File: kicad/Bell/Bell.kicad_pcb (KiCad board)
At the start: 2 copper layers, 50.6 x 40.5 mm, 14 parts, among them J1 Jack-DC, Q1 Q_NMOS_GDS, U1 NodeMCUv3

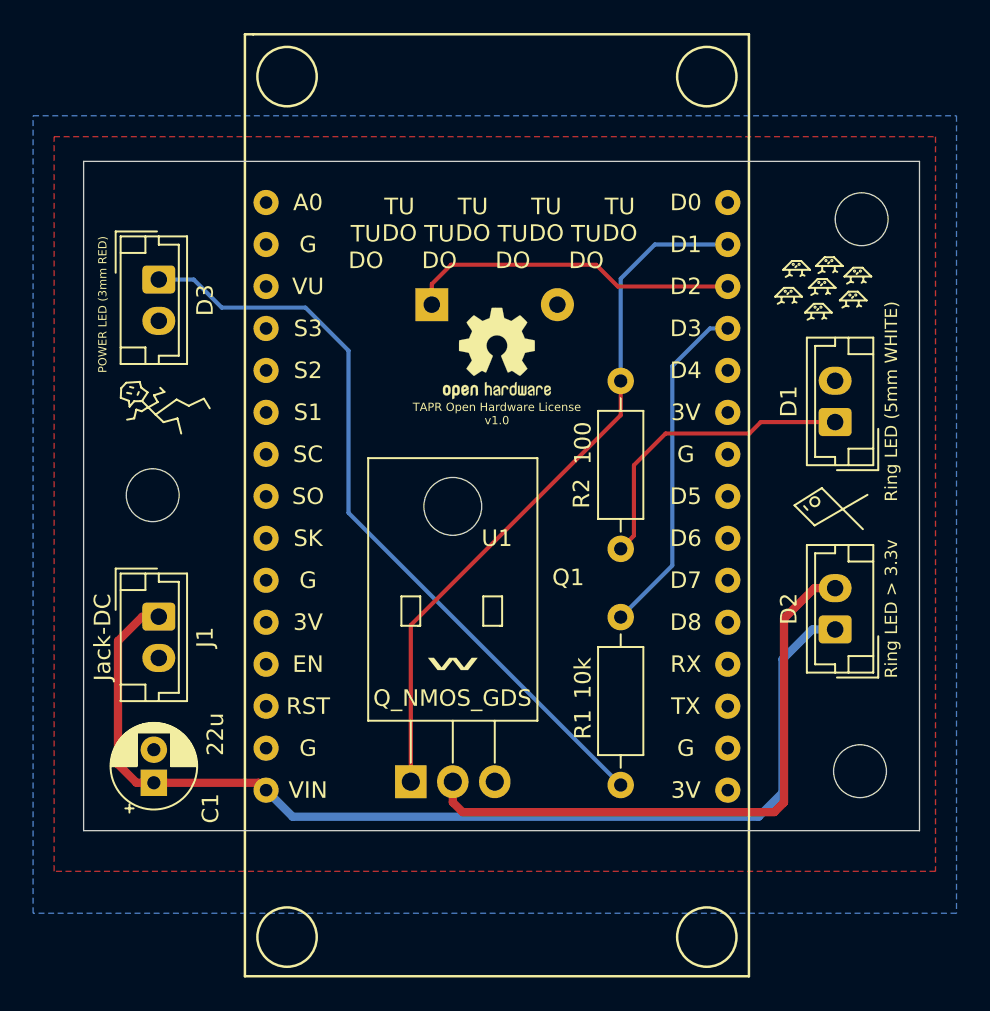
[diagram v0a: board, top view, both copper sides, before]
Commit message: Git: Ignore kicad backups and cache files
Signed-off-by: CTXz <ctx.xda@gmail.com>
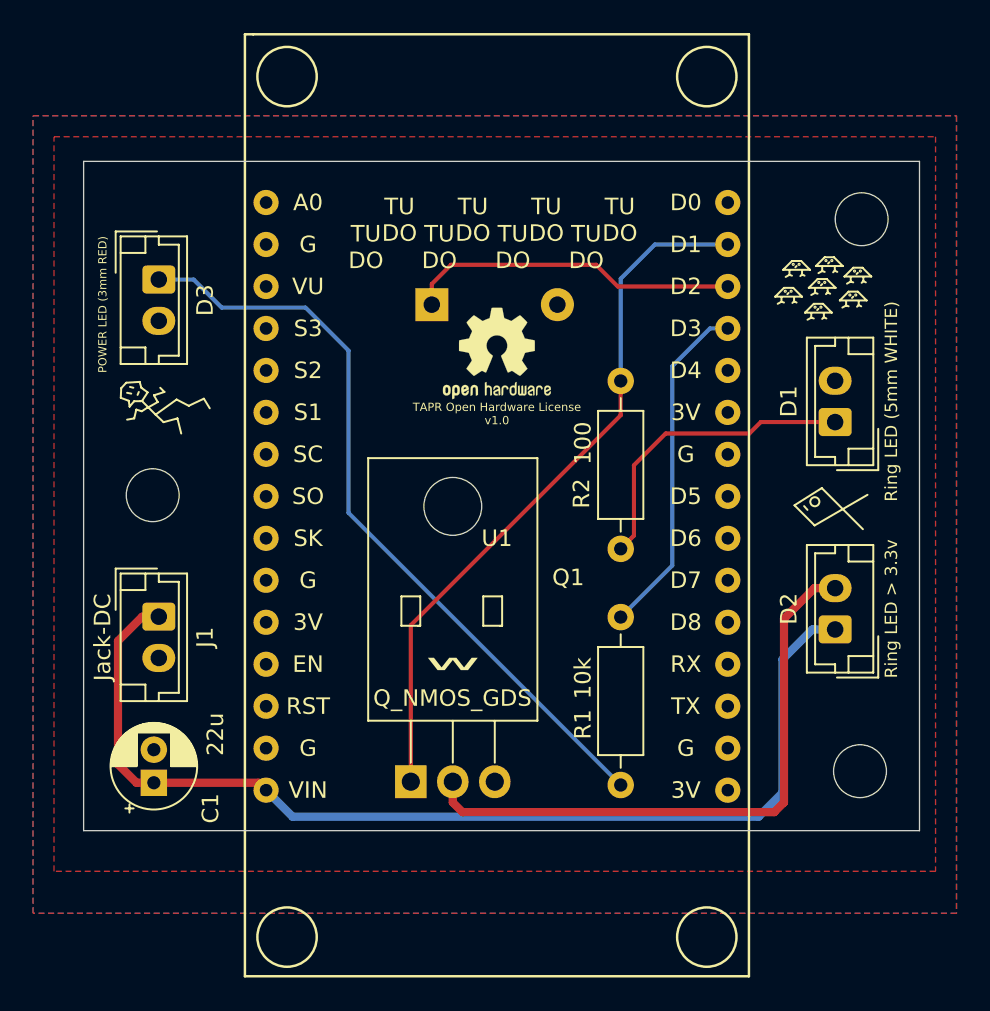
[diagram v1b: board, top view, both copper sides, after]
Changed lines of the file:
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@@
   (segment (start 135.419999 91.446701) (end 135.419999 87.185601) (width 0.25) (layer "F.Cu") (net 27))
   (segment (start 143.09806 84.57484) (end 142.4051 85.2678) (width 0.25) (layer "F.Cu") (net 27))
+  (zone (net 1) (net_name "GND") (layers F&B.Cu) (hatch edge 0.508)
+    (connect_pads (clearance 0.508))
+    (min_thickness 0.254) (filled_areas_thickness no)
+    (fill yes (thermal_gap 0.508) (thermal_bridge_width 0.508))
+    (polygon
+      (pts
+        (xy 154.94 114.3)
+        (xy 99.06 114.3)
+        (xy 99.06 66.04)
+        (xy 154.94 66.04)
+      )
+    )
+  )
   (zone (net 1) (net_name "GND") (layer "F.Cu") (hatch edge 0.508)
     (connect_pads (clearance 0.508))
-    (min_thickness 0.254)
+    (min_thickness 0.254) (filled_areas_thickness no)
     (fill yes (thermal_gap 0.508) (thermal_bridge_width 0.508))
     (polygon
@@
       )
     )
-  )
-  (zone (net 1) (net_name "GND") (layer "B.Cu") (hatch edge 0.508)
-    (connect_pads (clearance 0.508))
-    (min_thickness 0.254)
-    (fill yes (thermal_gap 0.508) (thermal_bridge_width 0.508))
-    (polygon
-      (pts
-        (xy 154.94 114.3)
-        (xy 99.06 114.3)
-        (xy 99.06 66.04)
-        (xy 154.94 66.04)
-      )
-    )
